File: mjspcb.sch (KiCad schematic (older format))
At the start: 37 parts, among them P1 2.7 - 6.0 VDC, P2 serial breakout, P3 I2C breakout, P4 GPS, P5 piezo, P6 BPW34, P7 electrodes, P8 perfboard breakout, P9 reset, Q1 STU60N3LH5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

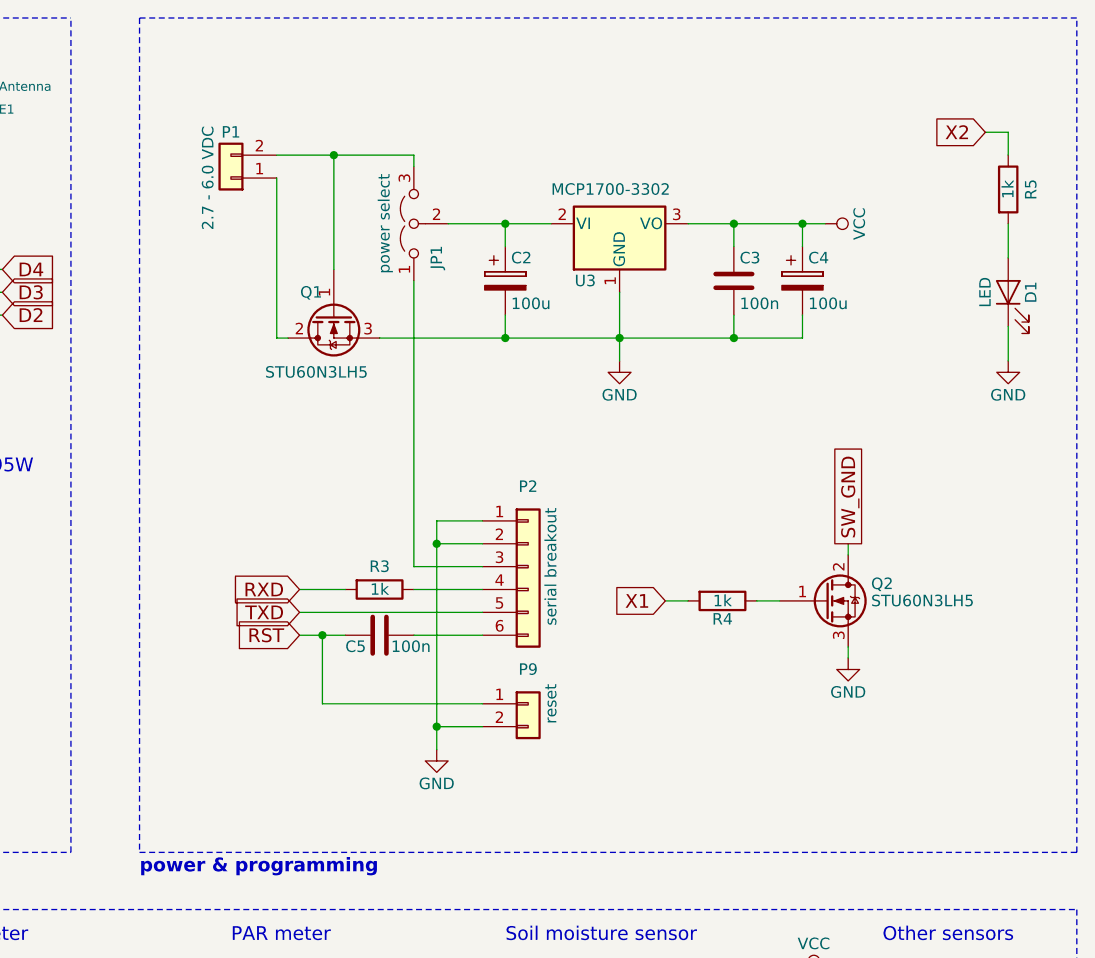
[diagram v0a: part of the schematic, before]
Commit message: Add DC plug and Lipo connector to schematic
These were in the board layout, but not in the schematic. This adds them
to the schematic, and sets the appropriate references in the layouted
footprints.

Note that the DC plug symbol has a different pin numbering than the
footprint currently in use, but the symbol does match the footprint set
in the schematic, so this should work out when the netlist is re-read in
the future.
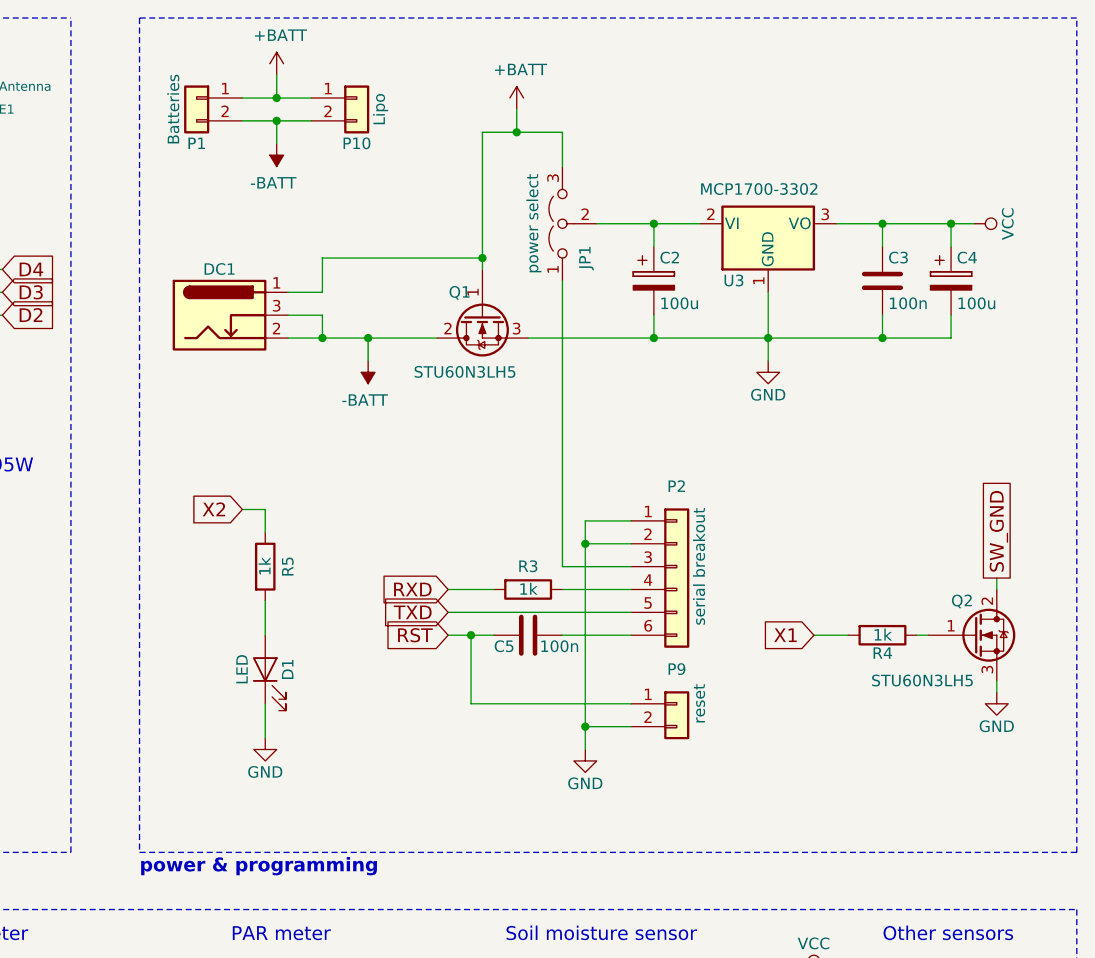
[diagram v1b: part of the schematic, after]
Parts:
- added DC1: 2.7 - 6.0 VDC, Connector_BarrelJack:BarrelJack_Wuerth_6941xx301002, symbol Connector:Barrel_Jack_Switch
- added P10: Lipo, Connector_JST:JST_PH_S2B-PH-K_1x02_P2.00mm_Horizontal, symbol Connector_Generic:Conn_01x02
- P1: value 2.7 - 6.0 VDC -> Batteries
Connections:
- net +BATT: now reaches P1.1 (Pin_1)
- net +BATT: now also JP1.3 (B), Q1.1 (G), DC1.1, P10.1 (Pin_1); no longer Q1.2 (D)
- new net -BATT: DC1.2, DC1.3, P1.2 (Pin_2), P10.2 (Pin_2), Q1.2 (D)
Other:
- moved on the sheet: C2, C3, C4, C5, D1, JP1, P1, P2, P9, Q1, Q2, R3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

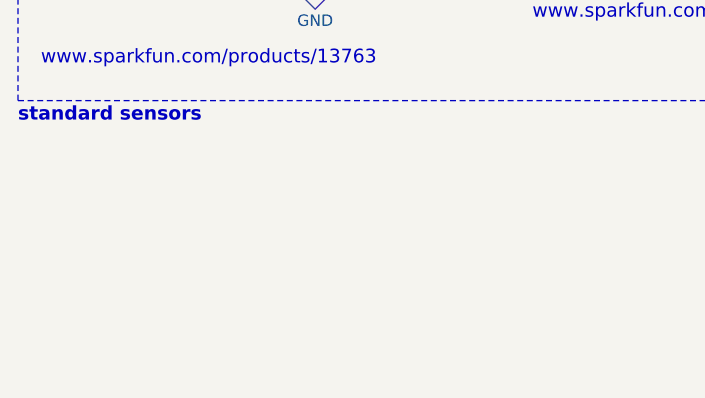
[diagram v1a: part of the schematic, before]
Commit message: Add mounting holes and logos to the schematic
This adds them and sets footprints, but does not update the board (not
even to update the REF properties, since I had too many other changes
already).
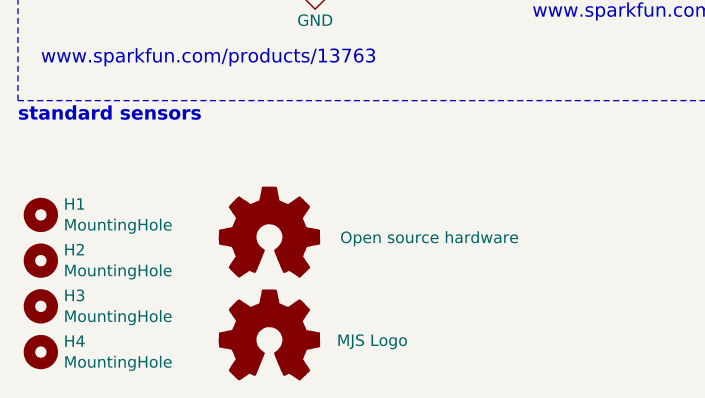
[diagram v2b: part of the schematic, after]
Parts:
- added H1, H2, H3, H4: MountingHole, MountingHole:MountingHole_3mm, symbol Mechanical:MountingHole
- added LOGO1: Open source hardware, Symbol:OSHW-Logo_5.7x6mm_SilkScreen, symbol Graphic:Logo_Open_Hardware_Small
- added LOGO2: MJS Logo, meetjestad:mjs, symbol Graphic:Logo_Open_Hardware_Small
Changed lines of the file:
@@
 	7600 1300 7600 1850
 Connection ~ 7750 1300
+$Comp
+L Mechanical:MountingHole H1
+U 1 1 5C1363B0
+P 900 6900
+F 0 "H1" H 1000 6946 50  0000 L CNN
+F 1 "MountingHole" H 1000 6855 50  0000 L CNN
+F 2 "MountingHole:MountingHole_3mm" H 900 6900 50  0001 C CNN
+F 3 "~" H 900 6900 50  0001 C CNN
+	1    900  6900
+	1    0    0    -1
+$EndComp
+$Comp
+L Mechanical:MountingHole H2
+U 1 1 5C136AFF
+P 900 7100
+F 0 "H2" H 1000 7146 50  0000 L CNN
+F 1 "MountingHole" H 1000 7055 50  0000 L CNN
+F 2 "MountingHole:MountingHole_3mm" H 900 7100 50  0001 C CNN
+F 3 "~" H 900 7100 50  0001 C CNN
+	1    900  7100
+	1    0    0    -1
+$EndComp
+$Comp
+L Mechanical:MountingHole H3
+U 1 1 5C137424
+P 900 7300
+F 0 "H3" H 1000 7346 50  0000 L CNN
+F 1 "MountingHole" H 1000 7255 50  0000 L CNN
+F 2 "MountingHole:MountingHole_3mm" H 900 7300 50  0001 C CNN
+F 3 "~" H 900 7300 50  0001 C CNN
+	1    900  7300
+	1    0    0    -1
+$EndComp
+$Comp
+L Mechanical:MountingHole H4
+U 1 1 5C13781B
+P 900 7500
+F 0 "H4" H 1000 7546 50  0000 L CNN
+F 1 "MountingHole" H 1000 7455 50  0000 L CNN
+F 2 "MountingHole:MountingHole_3mm" H 900 7500 50  0001 C CNN
+F 3 "~" H 900 7500 50  0001 C CNN
+	1    900  7500
+	1    0    0    -1
+$EndComp
+$Comp
+L Graphic:Logo_Open_Hardware_Small LOGO1
+U 1 1 5C138248
+P 1900 7000
+F 0 "LOGO1" H 1900 7275 50  0001 C CNN
+F 1 "Open source hardware" H 2600 7000 50  0000 C CNN
+F 2 "Symbol:OSHW-Logo_5.7x6mm_SilkScreen" H 1900 7000 50  0001 C CNN
+F 3 "~" H 1900 7000 50  0001 C CNN
+	1    1900 7000
+	1    0    0    -1
+$EndComp
+$Comp
+L Graphic:Logo_Open_Hardware_Small LOGO2
+U 1 1 5C138C4E
+P 1900 7450
+F 0 "LOGO2" H 1900 7725 50  0001 C CNN
+F 1 "MJS Logo" H 2350 7450 50  0000 C CNN
+F 2 "meetjestad:mjs" H 1900 7450 50  0001 C CNN
+F 3 "~" H 1900 7450 50  0001 C CNN
+	1    1900 7450
+	1    0    0    -1
+$EndComp
 $EndSCHEMATC

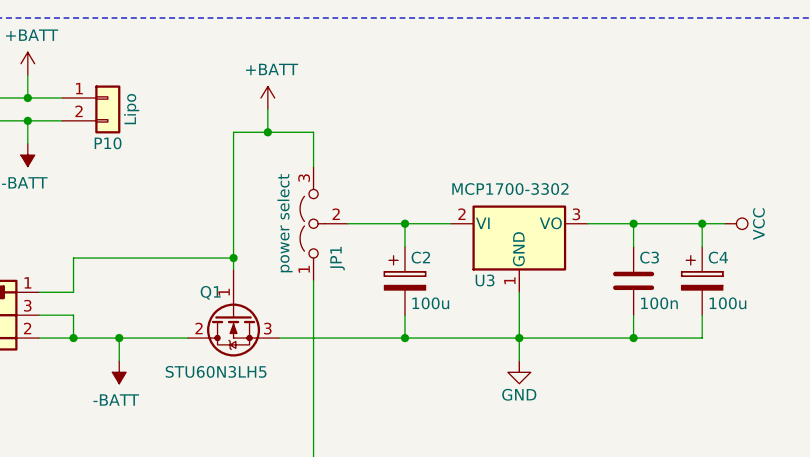
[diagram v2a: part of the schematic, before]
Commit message: Convert board layout to KiCad 5
This replaces all footprints with new versions from KiCad 5. Some
positions and labeling as changed, so this updates everything to match
the original layout for the most part. Some footprints (barrel jack,
regulator, battery holder, solder jumpers, perfboard "connector") are
slightly different. In particualr the battery holde slightly changes the
mounting hole position and size, so this might need to be changed back
later.

The only footprints that are still used from the project library are the
logo, all others are removed. All components are also in the schematic,
except for the perfboard individiual pins (which also do not have any
external footprint they refer to).

The GPS connector footprint has holes that are slightly (0.05mm) bigger,
which should make it easier to fit the connector.
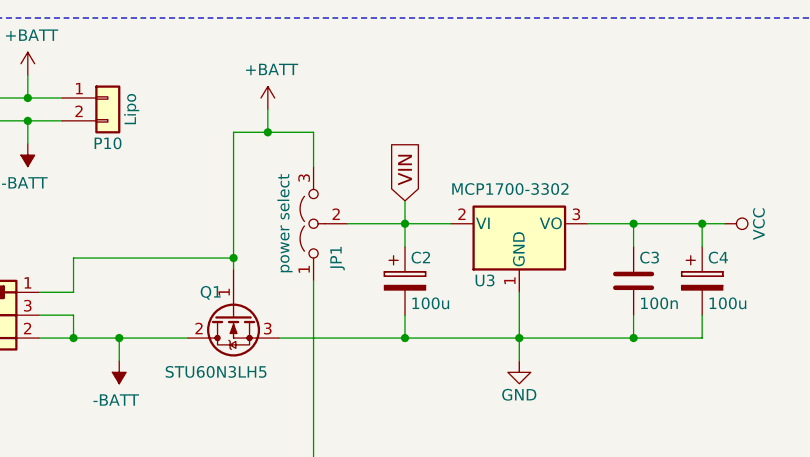
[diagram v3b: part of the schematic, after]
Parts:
- JP2, JP3: footprint Jumper:SolderJumper-3_P1.3mm_Bridged12_Pad1.0x1.5mm -> Jumper:SolderJumper-3_P1.3mm_Bridged12_RoundedPad1.0x1.5mm_NumberLabels
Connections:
- net VIN: now reaches C2.1, JP1.2 (C), U3.2 (VI)
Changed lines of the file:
@@
 F 0 "JP2" H 1900 5450 60  0000 C CNN
 F 1 "V1" H 1800 5250 60  0001 C CNN
-F 2 "Jumper:SolderJumper-3_P1.3mm_Bridged12_Pad1.0x1.5mm" H 1750 5350 60  0001 C CNN
+F 2 "Jumper:SolderJumper-3_P1.3mm_Bridged12_RoundedPad1.0x1.5mm_NumberLabels" H 1750 5350 60  0001 C CNN
 F 3 "" H 1900 5450 60  0001 C CNN
 	1    1900 5350
@@
 F 0 "JP3" H 2300 5450 60  0000 C CNN
 F 1 "V2" H 2200 5250 60  0001 C CNN
-F 2 "Jumper:SolderJumper-3_P1.3mm_Bridged12_Pad1.0x1.5mm" H 2150 5350 60  0001 C CNN
+F 2 "Jumper:SolderJumper-3_P1.3mm_Bridged12_RoundedPad1.0x1.5mm_NumberLabels" H 2150 5350 60  0001 C CNN
 F 3 "" H 2300 5450 60  0001 C CNN
 	1    2300 5350
@@
 	1    0    0    -1
 $EndComp
+Text GLabel 8350 1600 1    60   Input ~ 0
+VIN
+Wire Wire Line
+	8350 1600 8350 1700
 $EndSCHEMATC

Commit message: Fix DRC errors in solder jumper footprint
This uses a modified solder jumper footprint that has a graphic polygon
rather than overlapping pads to connect the default pins, which prevents
DRC errors. See: https://github.com/KiCad/kicad-footprints/issues/1165
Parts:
- JP2, JP3: footprint Jumper:SolderJumper-3_P1.3mm_Bridged12_RoundedPad1.0x1.5mm_NumberLabels -> meetjestad:SolderJumper-3_P1.3mm_Bridged12_RoundedPad1.0x1.5mm_NumberLabels
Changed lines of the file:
@@
 F 0 "JP2" H 1900 5450 60  0000 C CNN
 F 1 "V1" H 1800 5250 60  0001 C CNN
-F 2 "Jumper:SolderJumper-3_P1.3mm_Bridged12_RoundedPad1.0x1.5mm_NumberLabels" H 1750 5350 60  0001 C CNN
+F 2 "meetjestad:SolderJumper-3_P1.3mm_Bridged12_RoundedPad1.0x1.5mm_NumberLabels" H 1750 5350 60  0001 C CNN
 F 3 "" H 1900 5450 60  0001 C CNN
 	1    1900 5350
@@
 F 0 "JP3" H 2300 5450 60  0000 C CNN
 F 1 "V2" H 2200 5250 60  0001 C CNN
-F 2 "Jumper:SolderJumper-3_P1.3mm_Bridged12_RoundedPad1.0x1.5mm_NumberLabels" H 2150 5350 60  0001 C CNN
+F 2 "meetjestad:SolderJumper-3_P1.3mm_Bridged12_RoundedPad1.0x1.5mm_NumberLabels" H 2150 5350 60  0001 C CNN
 F 3 "" H 2300 5450 60  0001 C CNN
 	1    2300 5350

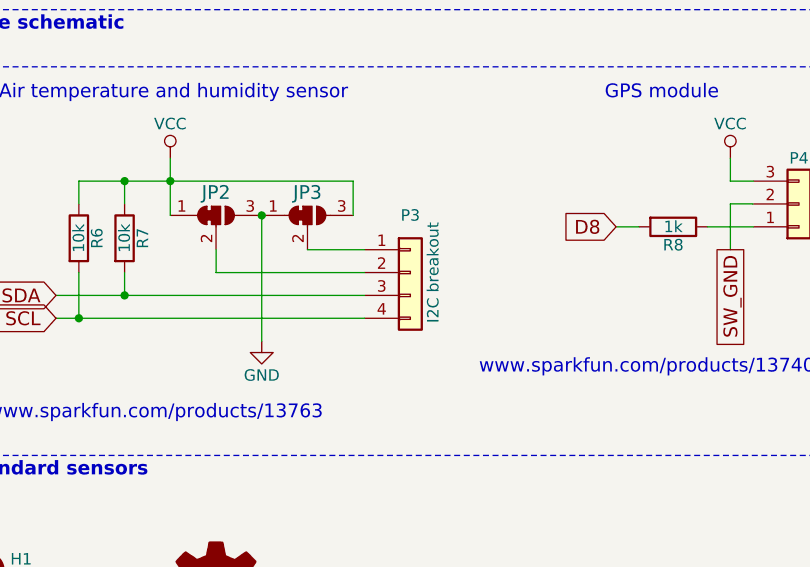
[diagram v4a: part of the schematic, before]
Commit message: Flip I²C socket
This swaps the pin numbering, to match the Grove pinout. The PCB layout
is also updated to flip the footprint, and move a few traces to make
room for the square pad on the other side.
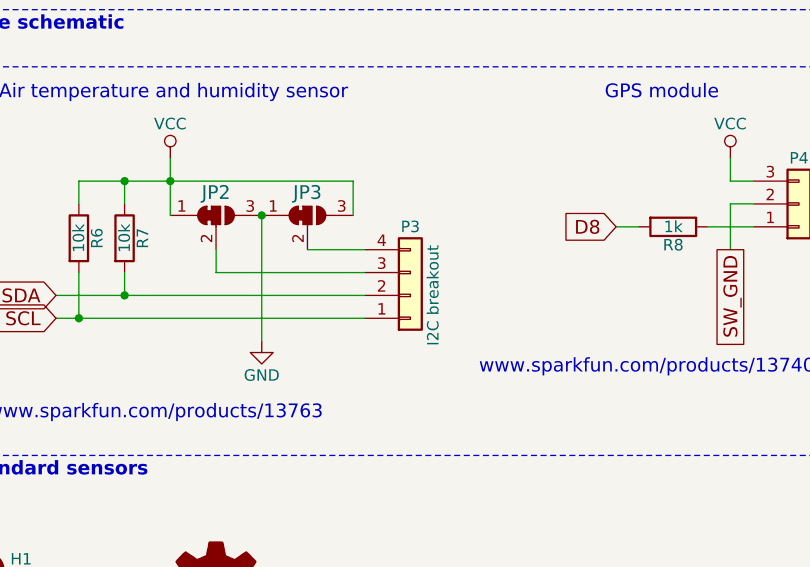
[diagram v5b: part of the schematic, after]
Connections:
- net SCL: now also P3.1 (Pin_1); no longer P3.4 (Pin_4)
- net SDA: now also P3.2 (Pin_2); no longer P3.3 (Pin_3)
- net at JP3.2 (C): now also P3.4 (Pin_4); no longer P3.1 (Pin_1)
- net at JP2.2 (C): now also P3.3 (Pin_3); no longer P3.2 (Pin_2)
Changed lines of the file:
@@
 L Connector_Generic:Conn_01x04 P3
 U 1 1 571A1889
-P 2750 5600
-F 0 "P3" H 2750 5850 50  0000 C CNN
-F 1 "I2C breakout" V 2850 5600 50  0000 C CNN
-F 2 "Connector_PinSocket_2.54mm:PinSocket_1x04_P2.54mm_Vertical" H 2750 5600 50  0001 C CNN
-F 3 "" H 2750 5600 50  0000 C CNN
-	1    2750 5600
-	1    0    0    -1
+P 2750 5700
+F 0 "P3" H 2750 5400 50  0000 C CNN
+F 1 "I2C breakout" V 2850 5700 50  0000 C CNN
+F 2 "Connector_PinSocket_2.54mm:PinSocket_1x04_P2.54mm_Vertical" H 2750 5700 50  0001 C CNN
+F 3 "" H 2750 5700 50  0000 C CNN
+	1    2750 5700
+	1    0    0    1
 $EndComp
 $Comp

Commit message: Replace I²C connector with a more sturdy one
This one has extra holes to plug in the sensor, so it can be mounted
lower and more stable. This also makes the board slightly longer at the
bottom to accomdate the new connector, and shorter at the top.
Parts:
- P3: footprint Connector_PinSocket_2.54mm:PinSocket_1x04_P2.54mm_Vertical -> meetjestad:Molex_KK-254_44812-0004_1x04_P2.54mm_Vertical
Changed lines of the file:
@@
 F 0 "P3" H 2750 5400 50  0000 C CNN
 F 1 "I2C breakout" V 2850 5700 50  0000 C CNN
-F 2 "Connector_PinSocket_2.54mm:PinSocket_1x04_P2.54mm_Vertical" H 2750 5700 50  0001 C CNN
+F 2 "meetjestad:Molex_KK-254_44812-0004_1x04_P2.54mm_Vertical" H 2750 5700 50  0001 C CNN
 F 3 "" H 2750 5700 50  0000 C CNN
 	1    2750 5700

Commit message: Replace 2-pin sensor connectors with KK254
These are latching, polarity protected connectors. This mostly changes
to silkscreen, though the pads are also slighly differently sized.
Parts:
- P5, P6, P7: footprint Connector_PinHeader_2.54mm:PinHeader_1x02_P2.54mm_Vertical -> Connector_Molex:Molex_KK-254_AE-6410-02A_1x02_P2.54mm_Vertical
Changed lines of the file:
@@
 F 0 "P5" H 6200 5250 50  0000 C CNN
 F 1 "piezo" V 6300 5100 50  0000 C CNN
-F 2 "Connector_PinHeader_2.54mm:PinHeader_1x02_P2.54mm_Vertical" H 6200 5100 50  0001 C CNN
+F 2 "Connector_Molex:Molex_KK-254_AE-6410-02A_1x02_P2.54mm_Vertical" H 6200 5100 50  0001 C CNN
 F 3 "" H 6200 5100 50  0000 C CNN
 	1    6200 5100
@@
 F 0 "P6" H 7300 5350 50  0000 C CNN
 F 1 "BPW34" V 7400 5200 50  0000 C CNN
-F 2 "Connector_PinHeader_2.54mm:PinHeader_1x02_P2.54mm_Vertical" H 7300 5200 50  0001 C CNN
+F 2 "Connector_Molex:Molex_KK-254_AE-6410-02A_1x02_P2.54mm_Vertical" H 7300 5200 50  0001 C CNN
 F 3 "" H 7300 5200 50  0000 C CNN
 	1    7300 5200
@@
 F 0 "P7" H 8800 5350 50  0000 C CNN
 F 1 "electrodes" V 8900 5200 50  0000 C CNN
-F 2 "Connector_PinHeader_2.54mm:PinHeader_1x02_P2.54mm_Vertical" H 8800 5200 50  0001 C CNN
+F 2 "Connector_Molex:Molex_KK-254_AE-6410-02A_1x02_P2.54mm_Vertical" H 8800 5200 50  0001 C CNN
 F 3 "" H 8800 5200 50  0000 C CNN
 	1    8800 5200
